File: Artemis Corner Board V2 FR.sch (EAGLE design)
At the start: 93 parts, among them Q1 BSS138, U1 OPA365AIDBVR, U2 ADS1232IPWR, U3 MCP2562, U4 TM4C123GH6PMI, U5 MCP2562, U6 LM3671MF-3.3/NOPB, U8 TPS562219, U9 FT232RL, Y1 16MHz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

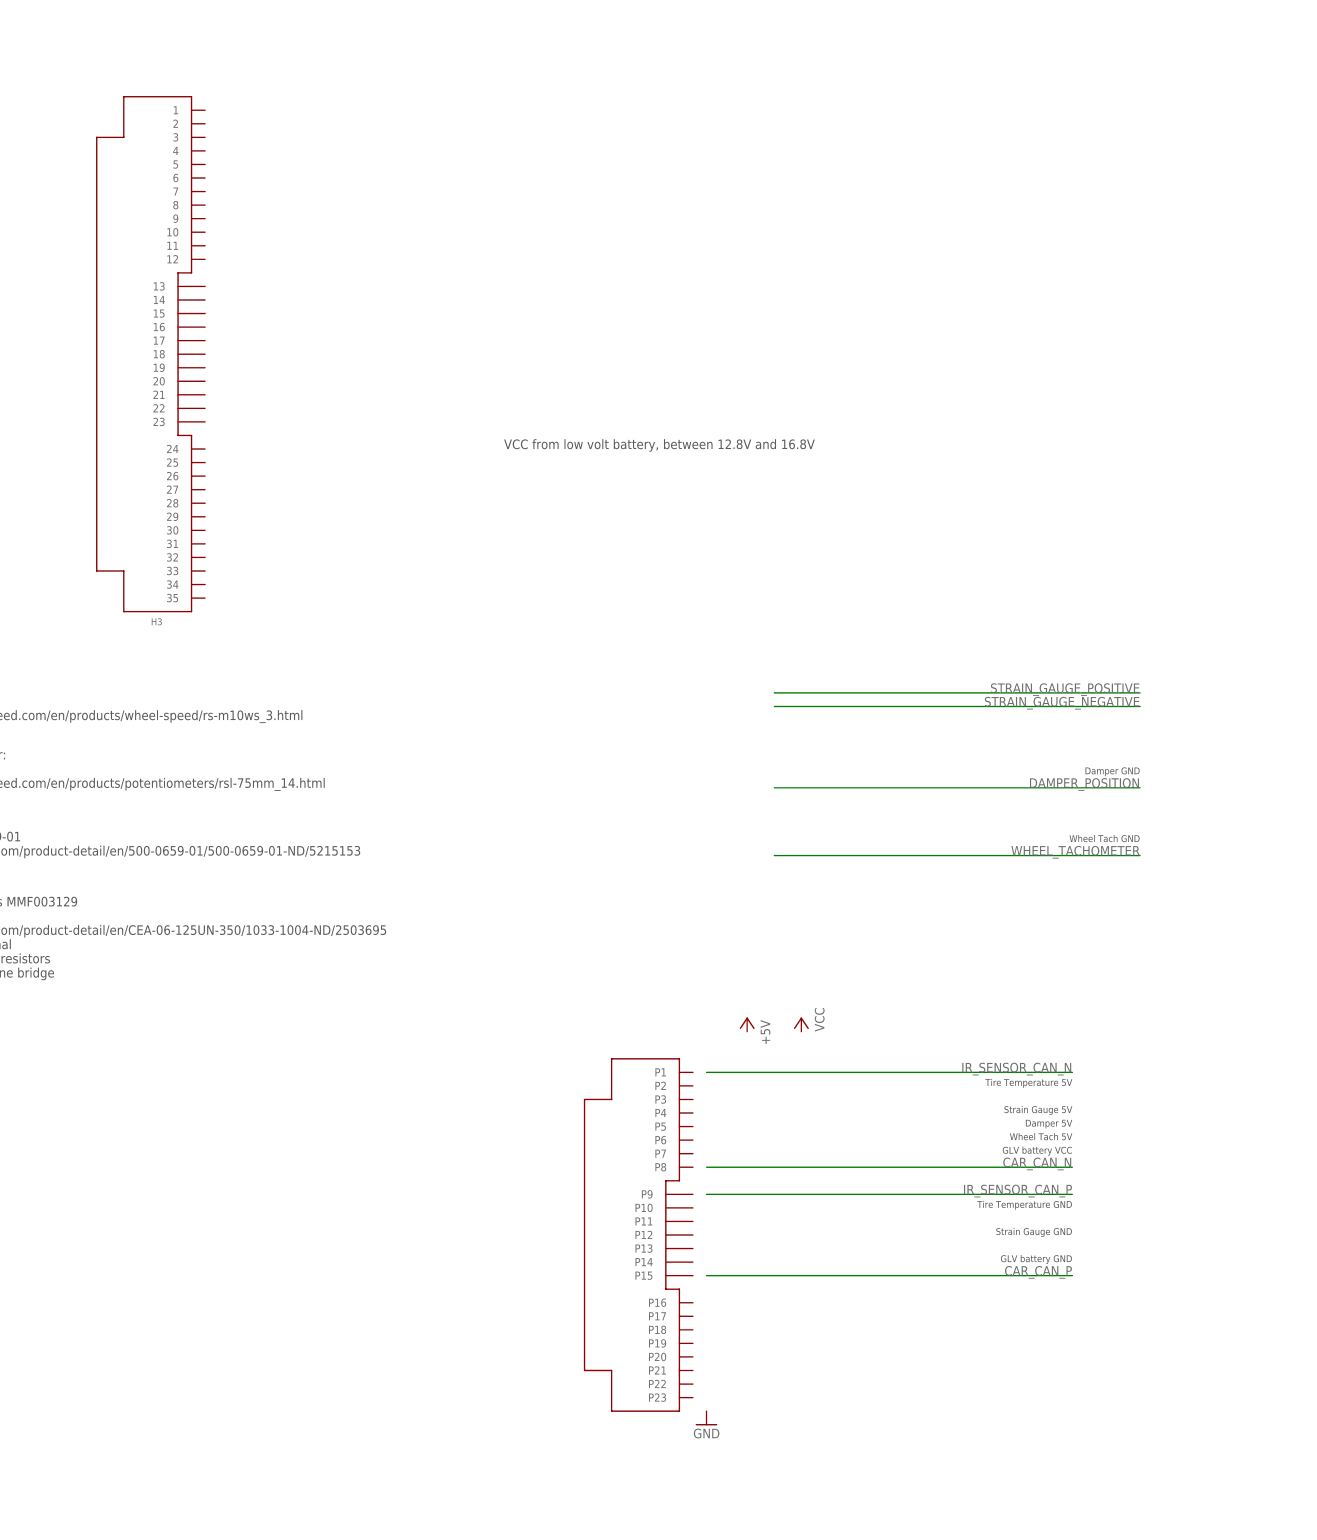
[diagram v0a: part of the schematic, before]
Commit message: Switched to 23-pin ampseal connector
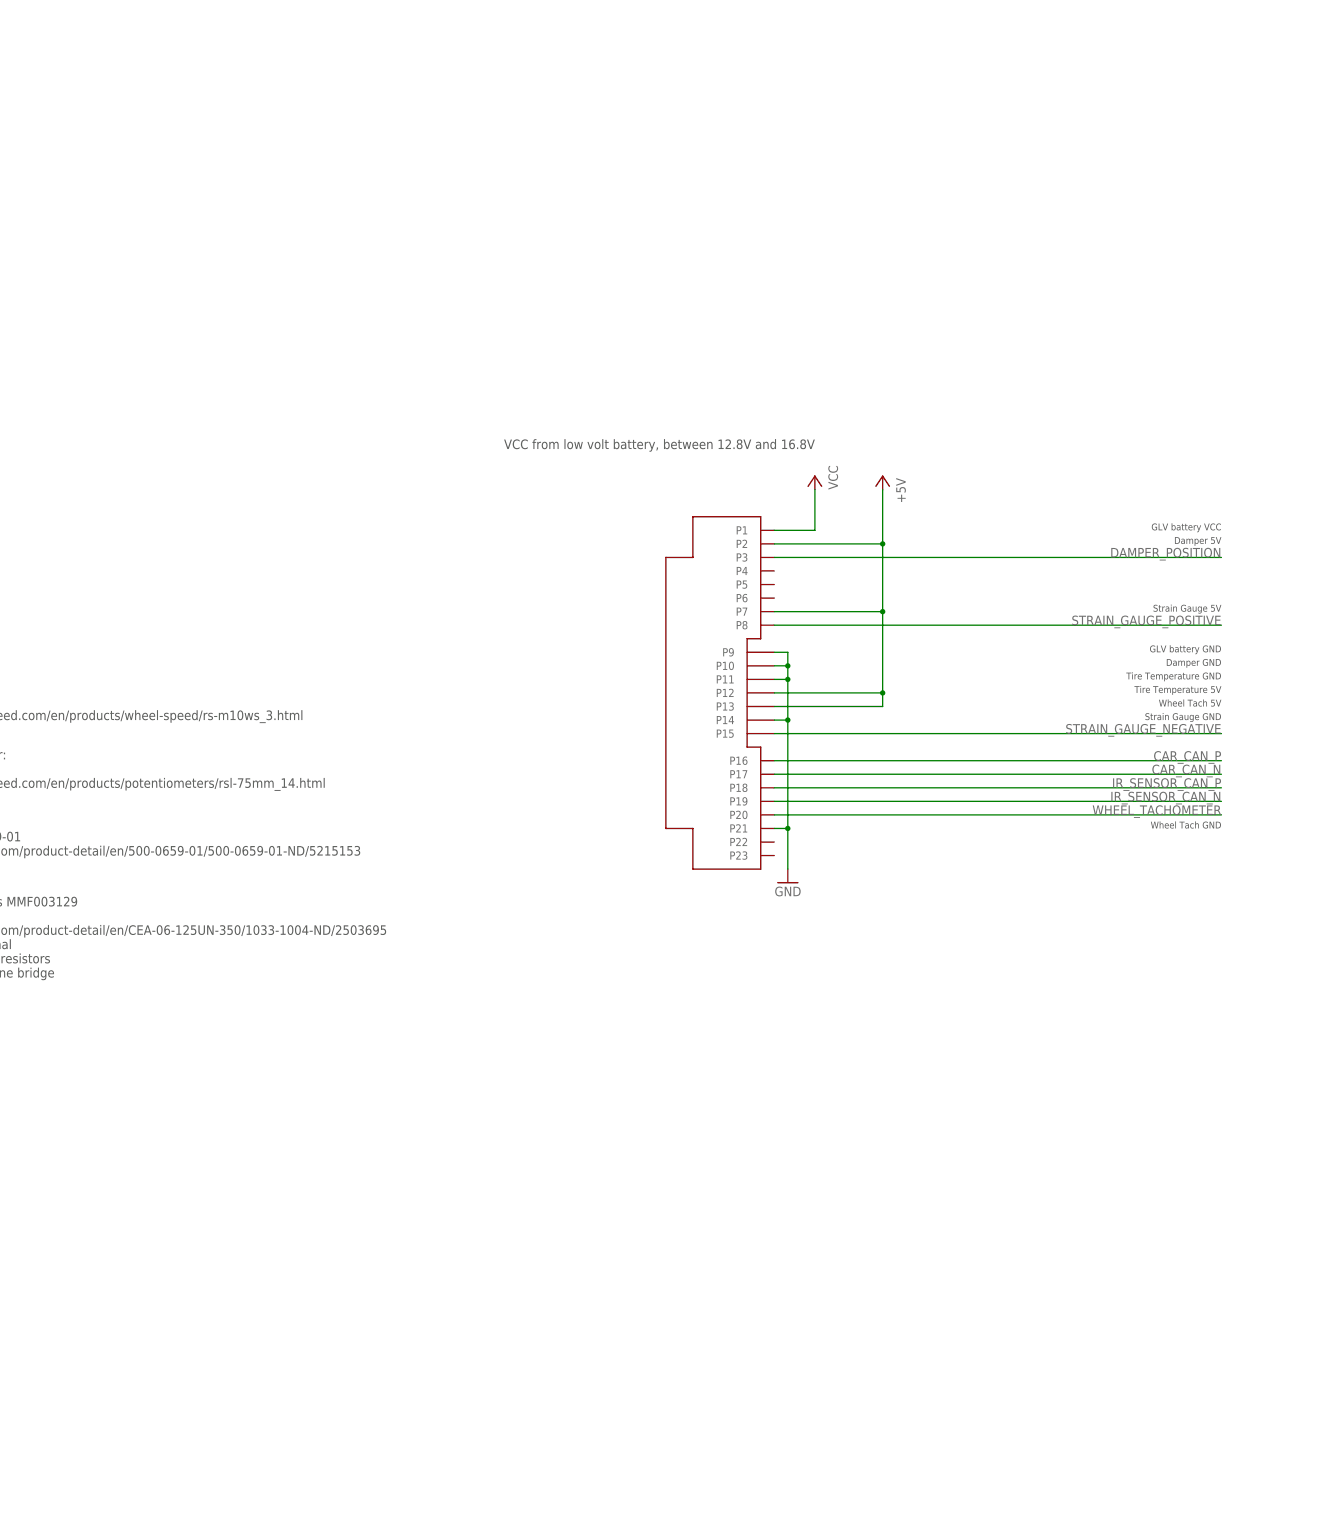
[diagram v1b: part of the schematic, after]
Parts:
- removed H3: 1-776231-1, FormE:1-776231-1
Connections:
- net +5V: now also H1.P12, H1.P13, H1.P2, H1.P7
- net CAR_CAN_N: now also H1.P17
- net CAR_CAN_P: now also H1.P16
- net DAMPER_POSITION: now also H1.P3
- net GND: now also H1.P10, H1.P11, H1.P14, H1.P21, H1.P9
- net IR_SENSOR_CAN_N: now also H1.P19
- net IR_SENSOR_CAN_P: now also H1.P18
- net STRAIN_GAUGE_NEGATIVE: now also H1.P15
- net STRAIN_GAUGE_POSITIVE: now also H1.P8
- net VCC: now also H1.P1
- net WHEEL_TACHOMETER: now also H1.P20
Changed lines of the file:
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@@
 <setting verticaltext="up"/>
 </settings>
-<grid distance="0.1" unitdist="inch" unit="inch" style="lines" multiple="1" display="no" altdistance="0.01" altunitdist="inch" altunit="inch"/>
+<grid distance="0.1" unitdist="inch" unit="inch" style="lines" multiple="1" display="yes" altdistance="0.01" altunitdist="inch" altunit="inch"/>
 <layers>
 <layer number="1" name="Top" color="4" fill="1" visible="no" active="no"/>
@@
 </part>
 <part name="+3V1" library="supply1" deviceset="+3V3" device=""/>
-<part name="H3" library="FormE" deviceset="1-776231-1" device="" value="1-776231-1"/>
 <part name="H1" library="FormE" deviceset="776228-4" device="" value="776228-4"/>
 </parts>
@@
 <text x="789.94" y="223.52" size="1.778" layer="91">25V or higher cap</text>
 <text x="756.92" y="254" size="1.778" layer="91">25V or higher cap</text>
-<text x="-523.24" y="63.5" size="1.27" layer="97" rot="MR0">Strain Gauge GND</text>
-<text x="-510.54" y="149.86" size="1.27" layer="97" rot="MR0">Damper GND</text>
-<text x="-510.54" y="137.16" size="1.27" layer="97" rot="MR0">Wheel Tach GND</text>
-<text x="-523.24" y="68.58" size="1.27" layer="97" rot="MR0">Tire Temperature GND</text>
-<text x="-523.24" y="91.44" size="1.27" layer="97" rot="MR0">Tire Temperature 5V</text>
-<text x="-523.24" y="81.28" size="1.27" layer="97" rot="MR0">Wheel Tach 5V</text>
-<text x="-523.24" y="83.82" size="1.27" layer="97" rot="MR0">Damper 5V</text>
-<text x="-523.24" y="86.36" size="1.27" layer="97" rot="MR0">Strain Gauge 5V</text>
+<text x="-495.3" y="160.02" size="1.27" layer="97" rot="MR0">Strain Gauge GND</text>
+<text x="-495.3" y="170.18" size="1.27" layer="97" rot="MR0">Damper GND</text>
+<text x="-495.3" y="139.7" size="1.27" layer="97" rot="MR0">Wheel Tach GND</text>
+<text x="-495.3" y="167.64" size="1.27" layer="97" rot="MR0">Tire Temperature GND</text>
+<text x="-495.3" y="165.1" size="1.27" layer="97" rot="MR0">Tire Temperature 5V</text>
+<text x="-495.3" y="162.56" size="1.27" layer="97" rot="MR0">Wheel Tach 5V</text>
+<text x="-495.3" y="193.04" size="1.27" layer="97" rot="MR0">Damper 5V</text>
+<text x="-495.3" y="180.34" size="1.27" layer="97" rot="MR0">Strain Gauge 5V</text>
 <text x="-264.16" y="231.14" size="1.778" layer="97">See TI's reference design: ADS1232REF
 Also read: http://www.ti.com/lit/ml/slyp163/slyp163.pdf</text>
@@
   350-ohm precision resistors
   to form a wheatstone bridge</text>
-<text x="-523.24" y="78.74" size="1.27" layer="97" rot="MR0">GLV battery VCC</text>
-<text x="-523.24" y="58.42" size="1.27" layer="97" rot="MR0">GLV battery GND</text>
+<text x="-495.3" y="195.58" size="1.27" layer="97" rot="MR0">GLV battery VCC</text>
+<text x="-495.3" y="172.72" size="1.27" layer="97" rot="MR0">GLV battery GND</text>
 <text x="264.16" y="210.82" size="1.778" layer="97" rot="MR0">NC</text>
 <text x="-205.74" y="139.7" size="1.778" layer="97">NC</text>
@@
 </plain>
 <instances>
-<instance part="P+1" gate="VCC" x="-574.04" y="104.14" rot="MR0"/>
-<instance part="GND1" gate="1" x="-591.82" y="27.94" rot="MR0"/>
-<instance part="P+2" gate="1" x="-584.2" y="104.14" rot="MR0"/>
+<instance part="P+1" gate="VCC" x="-571.5" y="205.74" rot="MR0"/>
+<instance part="GND1" gate="1" x="-576.58" y="129.54" rot="MR0"/>
+<instance part="P+2" gate="1" x="-558.8" y="205.74" rot="MR0"/>
 <instance part="GND46" gate="1" x="782.32" y="160.02"/>
 <instance part="GND53" gate="1" x="838.2" y="160.02"/>
@@
 </instance>
 <instance part="+3V1" gate="G$1" x="850.9" y="185.42"/>
-<instance part="H3" gate="G$1" x="-701.04" y="228.6"/>
-<instance part="H1" gate="G$2" x="-609.6" y="63.5"/>
+<instance part="H1" gate="G$2" x="-594.36" y="165.1"/>
 </instances>
 <busses>
@@
 <wire x1="838.2" y1="165.1" x2="838.2" y2="162.56" width="0.1524" layer="91"/>
 </segment>
+<segment>
+<pinref part="H1" gate="G$2" pin="P9"/>
+<pinref part="GND1" gate="1" pin="GND"/>
+<wire x1="-579.12" y1="172.72" x2="-576.58" y2="172.72" width="0.1524" layer="91"/>
+<wire x1="-576.58" y1="172.72" x2="-576.58" y2="170.18" width="0.1524" layer="91"/>
+<pinref part="H1" gate="G$2" pin="P10"/>
+<wire x1="-576.58" y1="170.18" x2="-576.58" y2="167.64" width="0.1524" layer="91"/>
+<wire x1="-576.58" y1="167.64" x2="-576.58" y2="160.02" width="0.1524" layer="91"/>
+<wire x1="-576.58" y1="160.02" x2="-576.58" y2="139.7" width="0.1524" layer="91"/>
+<wire x1="-576.58" y1="139.7" x2="-576.58" y2="132.08" width="0.1524" layer="91"/>
+<wire x1="-579.12" y1="170.18" x2="-576.58" y2="170.18" width="0.1524" layer="91"/>
+<junction x="-576.58" y="170.18"/>
+<pinref part="H1" gate="G$2" pin="P11"/>
+<wire x1="-579.12" y1="167.64" x2="-576.58" y2="167.64" width="0.1524" layer="91"/>
+<junction x="-576.58" y="167.64"/>
+<pinref part="H1" gate="G$2" pin="P14"/>
+<wire x1="-579.12" y1="160.02" x2="-576.58" y2="160.02" width="0.1524" layer="91"/>
+<junction x="-576.58" y="160.02"/>
+<pinref part="H1" gate="G$2" pin="P21"/>
+<wire x1="-579.12" y1="139.7" x2="-576.58" y2="139.7" width="0.1524" layer="91"/>
+<junction x="-576.58" y="139.7"/>
+</segment>
 </net>
 <net name="VCC" class="0">
@@
 <junction x="820.42" y="251.46"/>
 </segment>
+<segment>
+<pinref part="H1" gate="G$2" pin="P1"/>
+<pinref part="P+1" gate="VCC" pin="VCC"/>
+<wire x1="-579.12" y1="195.58" x2="-571.5" y2="195.58" width="0.1524" layer="91"/>
+<wire x1="-571.5" y1="195.58" x2="-571.5" y2="203.2" width="0.1524" layer="91"/>
+</segment>
 </net>
 <net name="+5V" class="0">
@@
 <junction x="769.62" y="175.26"/>
 </segment>
+<segment>
+<pinref part="H1" gate="G$2" pin="P2"/>
+<pinref part="P+2" gate="1" pin="+5V"/>
+<wire x1="-579.12" y1="193.04" x2="-558.8" y2="193.04" width="0.1524" layer="91"/>
+<wire x1="-558.8" y1="193.04" x2="-558.8" y2="203.2" width="0.1524" layer="91"/>
+<pinref part="H1" gate="G$2" pin="P12"/>
+<wire x1="-579.12" y1="165.1" x2="-558.8" y2="165.1" width="0.1524" layer="91"/>
+<wire x1="-558.8" y1="165.1" x2="-558.8" y2="180.34" width="0.1524" layer="91"/>
+<junction x="-558.8" y="193.04"/>
+<pinref part="H1" gate="G$2" pin="P13"/>
+<wire x1="-558.8" y1="180.34" x2="-558.8" y2="193.04" width="0.1524" layer="91"/>
+<wire x1="-579.12" y1="162.56" x2="-558.8" y2="162.56" width="0.1524" layer="91"/>
+<wire x1="-558.8" y1="162.56" x2="-558.8" y2="165.1" width="0.1524" layer="91"/>
+<junction x="-558.8" y="165.1"/>
+<pinref part="H1" gate="G$2" pin="P7"/>
+<wire x1="-579.12" y1="180.34" x2="-558.8" y2="180.34" width="0.1524" layer="91"/>
+<junction x="-558.8" y="180.34"/>
+</segment>
 </net>
 <net name="CAR_CAN_TX" class="0">
@@
 <net name="CAR_CAN_P" class="1">
 <segment>
-<wire x1="-591.82" y1="55.88" x2="-523.24" y2="55.88" width="0.1524" layer="91"/>
-<label x="-523.24" y="55.88" size="1.778" layer="95" rot="MR0"/>
+<wire x1="-579.12" y1="152.4" x2="-495.3" y2="152.4" width="0.1524" layer="91"/>
+<label x="-495.3" y="152.4" size="1.778" layer="95" rot="MR0"/>
+<pinref part="H1" gate="G$2" pin="P16"/>
 </segment>
 <segment>
@@
 </segment>
 <segment>
-<wire x1="-579.12" y1="165.1" x2="-510.54" y2="165.1" width="0.1524" layer="91"/>
-<label x="-510.54" y="165.1" size="1.778" layer="95" rot="MR0"/>
+<wire x1="-579.12" y1="177.8" x2="-495.3" y2="177.8" width="0.1524" layer="91"/>
+<label x="-495.3" y="177.8" size="1.778" layer="95" rot="MR0"/>
+<pinref part="H1" gate="G$2" pin="P8"/>
 </segment>
 </net>
@@
 </segment>
 <segment>
-<wire x1="-579.12" y1="162.56" x2="-510.54" y2="162.56" width="0.1524" layer="91"/>
-<label x="-510.54" y="162.56" size="1.778" layer="95" rot="MR0"/>
+<wire x1="-579.12" y1="157.48" x2="-495.3" y2="157.48" width="0.1524" layer="91"/>
+<label x="-495.3" y="157.48" size="1.778" layer="95" rot="MR0"/>
+<pinref part="H1" gate="G$2" pin="P15"/>
 </segment>
 </net>
 <net name="CAR_CAN_N" class="1">
 <segment>
-<wire x1="-591.82" y1="76.2" x2="-523.24" y2="76.2" width="0.1524" layer="91"/>
-<label x="-523.24" y="76.2" size="1.778" layer="95" rot="MR0"/>
+<wire x1="-579.12" y1="149.86" x2="-495.3" y2="149.86" width="0.1524" layer="91"/>
+<label x="-495.3" y="149.86" size="1.778" layer="95" rot="MR0"/>
+<pinref part="H1" gate="G$2" pin="P17"/>
 </segment>
 <segment>
@@
 </segment>
 <segment>
-<wire x1="-591.82" y1="71.12" x2="-523.24" y2="71.12" width="0.1524" layer="91"/>
-<label x="-523.24" y="71.12" size="1.778" layer="95" rot="MR0"/>
+<wire x1="-579.12" y1="147.32" x2="-495.3" y2="147.32" width="0.1524" layer="91"/>
+<label x="-495.3" y="147.32" size="1.778" layer="95" rot="MR0"/>
+<pinref part="H1" gate="G$2" pin="P18"/>
 </segment>
 </net>
@@
 </segment>
 <segment>
-<wire x1="-591.82" y1="93.98" x2="-523.24" y2="93.98" width="0.1524" layer="91"/>
-<label x="-523.24" y="93.98" size="1.778" layer="95" rot="MR0"/>
+<wire x1="-579.12" y1="144.78" x2="-495.3" y2="144.78" width="0.1524" layer="91"/>
+<label x="-495.3" y="144.78" size="1.778" layer="95" rot="MR0"/>
+<pinref part="H1" gate="G$2" pin="P19"/>
 </segment>
 </net>
@@
 <net name="DAMPER_POSITION" class="0">
 <segment>
-<wire x1="-579.12" y1="147.32" x2="-510.54" y2="147.32" width="0.1524" layer="91"/>
-<label x="-510.54" y="147.32" size="1.778" layer="95" rot="MR0"/>
+<wire x1="-579.12" y1="190.5" x2="-495.3" y2="190.5" width="0.1524" layer="91"/>
+<label x="-495.3" y="190.5" size="1.778" layer="95" rot="MR0"/>
+<pinref part="H1" gate="G$2" pin="P3"/>
 </segment>
 <segment>
@@
 <net name="WHEEL_TACHOMETER" class="0">
 <segment>
-<label x="-510.54" y="134.62" size="1.778" layer="95" rot="MR0"/>
-<wire x1="-579.12" y1="134.62" x2="-510.54" y2="134.62" width="0.1524" layer="91"/>
-</segment>
-<segment>
+<label x="-495.3" y="142.24" size="1.778" layer="95" rot="MR0"/>
+<wire x1="-579.12" y1="142.24" x2="-495.3" y2="142.24" width="0.1524" layer="91"/>
+<pinref part="H1" gate="G$2" pin="P20"/>
+</segment>
+<segment>

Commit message: Routed everything except the usb components, which may get removed.
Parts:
- removed JP1: (no value), pinhead:PINHD-1X2
- S1: value TE-FSM4JSMATR -> 147873-2; device FormE:TE-FSM4JSMATR -> FormE:TE-147873-2; PARTNO FSM4JSMATR -> 147873-2
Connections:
- net STRAIN_GAUGE_NEGATIVE renamed STRAIN_GAUGE_N
- net STRAIN_GAUGE_POSITIVE renamed STRAIN_GAUGE_P
- removed net N$19: JP1.2, U2.AINP2
- removed net N$9: JP1.1, U2.AINN2
- net CAR_CAN_N: now also H1.P16; no longer H1.P17
- net CAR_CAN_P: now also H1.P17; no longer H1.P16
- net CAR_CAN_RX: now also U4IO.PA0/CAN1RX/U0RX; no longer U4IO.PF0/C0O/CAN0RX/M1PWM4/NMI/PHA0/SSI1RX/T0CCP0/U1RTS
- net CAR_CAN_TX: now also U4IO.PA1/CAN1TX/U0TX; no longer U4IO.PF3/CAN0TX/M1PWM7/SSI1FSS/T1CCP1/TRCLK
- net GND: now also S1.1; no longer S1.3, S1.4
- net IR_SENSOR_CAN_N: now also H1.P18; no longer H1.P19
- net IR_SENSOR_CAN_P: now also H1.P19; no longer H1.P18
- net N$10: now also CF3.1; no longer CF3.3
- net N$12: now also CF4.3; no longer CF4.1
- net N$13: now also CF3.3; no longer CF3.1
- net N$18: now also CF4.1; no longer CF4.3
- net N$7: no longer S1.1
- net SENSOR_CAN_RX: now also U4IO.PF0/C0O/CAN0RX/M1PWM4/NMI/PHA0/SSI1RX/T0CCP0/U1RTS; no longer U4IO.PA0/CAN1RX/U0RX
- net SENSOR_CAN_TX: now also U4IO.PF3/CAN0TX/M1PWM7/SSI1FSS/T1CCP1/TRCLK; no longer U4IO.PA1/CAN1TX/U0TX
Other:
- moved on the sheet: C13, C14, C30, C31, R11, R14, U3, U5

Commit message: ERC/DRC fixes. This still needs to be mechanically reviewed
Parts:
- L1: value (none) -> 2.2uH
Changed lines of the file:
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@@
 <setting verticaltext="up"/>
 </settings>
-<grid distance="0.1" unitdist="inch" unit="inch" style="lines" multiple="1" display="yes" altdistance="0.01" altunitdist="inch" altunit="inch"/>
+<grid distance="0.1" unitdist="inch" unit="inch" style="lines" multiple="1" display="no" altdistance="0.01" altunitdist="inch" altunit="inch"/>
 <layers>
 <layer number="1" name="Top" color="4" fill="1" visible="no" active="no"/>
@@
 <part name="C40" library="rcl" deviceset="C-US" device="C0805" value="10uF"/>
 <part name="GND49" library="supply1" deviceset="GND" device=""/>
-<part name="L1" library="FormE" deviceset="L0805" device="">
+<part name="L1" library="FormE" deviceset="L0805" device="" value="2.2uH">
 <attribute name="PARTNO" value="74479775222"/>
 </part>
@@
 <text x="264.16" y="210.82" size="1.778" layer="97" rot="MR0">NC</text>
 <text x="-205.74" y="139.7" size="1.778" layer="97">NC</text>
-<text x="810.26" y="172.72" size="1.778" layer="97">74479775222</text>
+<text x="810.26" y="170.18" size="1.778" layer="97">74479775222</text>
 </plain>
 <instances>
